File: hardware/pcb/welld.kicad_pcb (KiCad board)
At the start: 2 copper layers, 80 x 55 mm, 74 parts, among them J1 LiPo, J10 PROG, J12 Solar, J2 USB-C, J3 U.FL, J4 4-20mA_1, J5 4-20mA_2, J6 DS18B20, J7 Spare, J8 I2C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

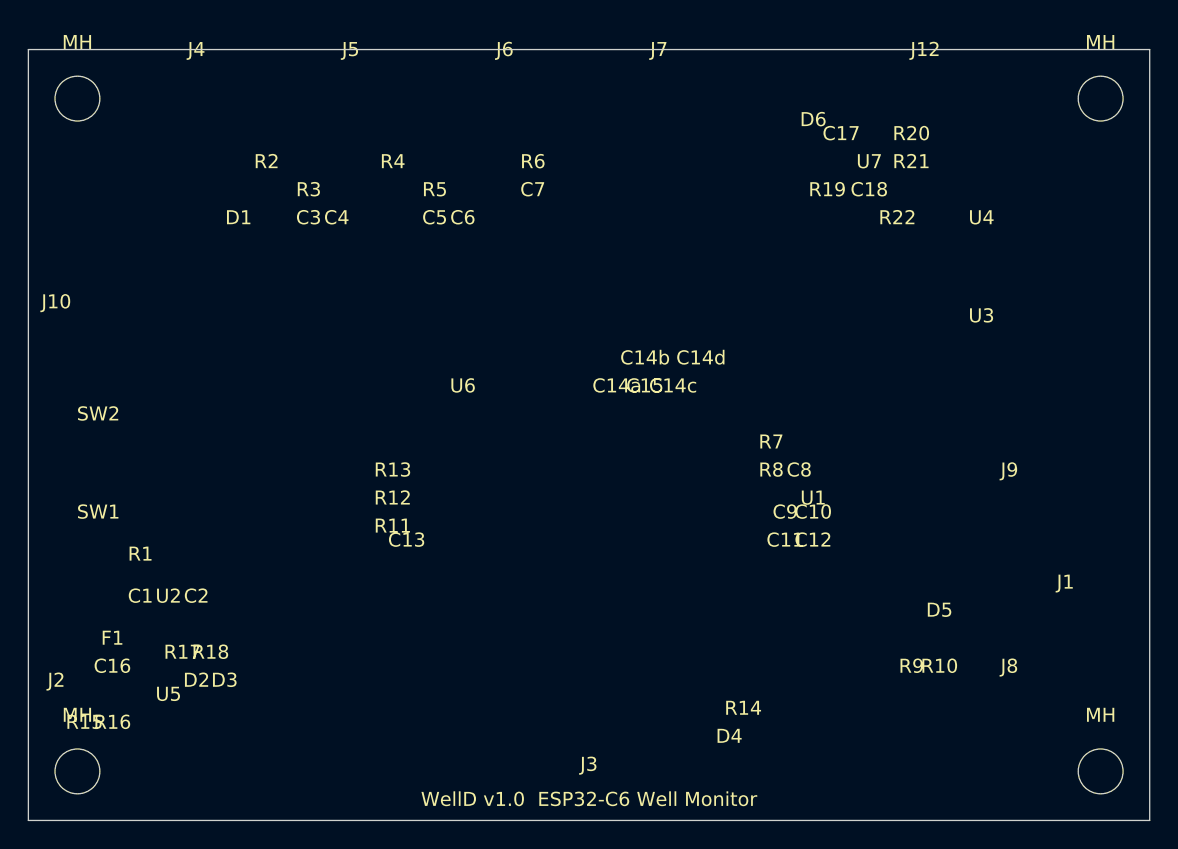
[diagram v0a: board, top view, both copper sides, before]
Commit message: Bring PCB schematic/layout in sync with the design docs
The KiCad generator was a revision behind the design notes and BOM:
the 12 V boost (U8), external ADC (U9), fuel gauge (U10), charger
interlock (Q1/Q2), boost inductor (L1), solar TVS (D8) and their
passives were documented but absent from welld.kicad_sch/.kicad_pcb.
Add them to generate_kicad.py, with TPS61023/ADS1115/MAX17048 symbols,
and regenerate.

Fix schematic/layout bugs: duplicate ESP32-C6 pin number, missing
GPIO14, stale DW01A symbol (now S-8261A), JST PH footprint on J1
(now JST XH), ADS1115 SOIC-8 footprint (now MSOP-10/VSSOP-10, the
correct 10-pin package), and two off-board component placements.
Add the missing TP4056 CE pull-up (R29).

Correct design.md errors: the R23/R24 boost-divider values, the D8
TVS protection claim, the reverse-polarity FET topology, the ESP32-C6
USB pin assignment, the ADS1115 channel/PGA description, and add a
GPIO15 strapping note and an MPPT diode-drop note.

Drop all revision language across the hardware docs and generators —
this is the single current design.

https://claude.ai/code/session_01QqBrArSSEuu1qysbVH7Nqt
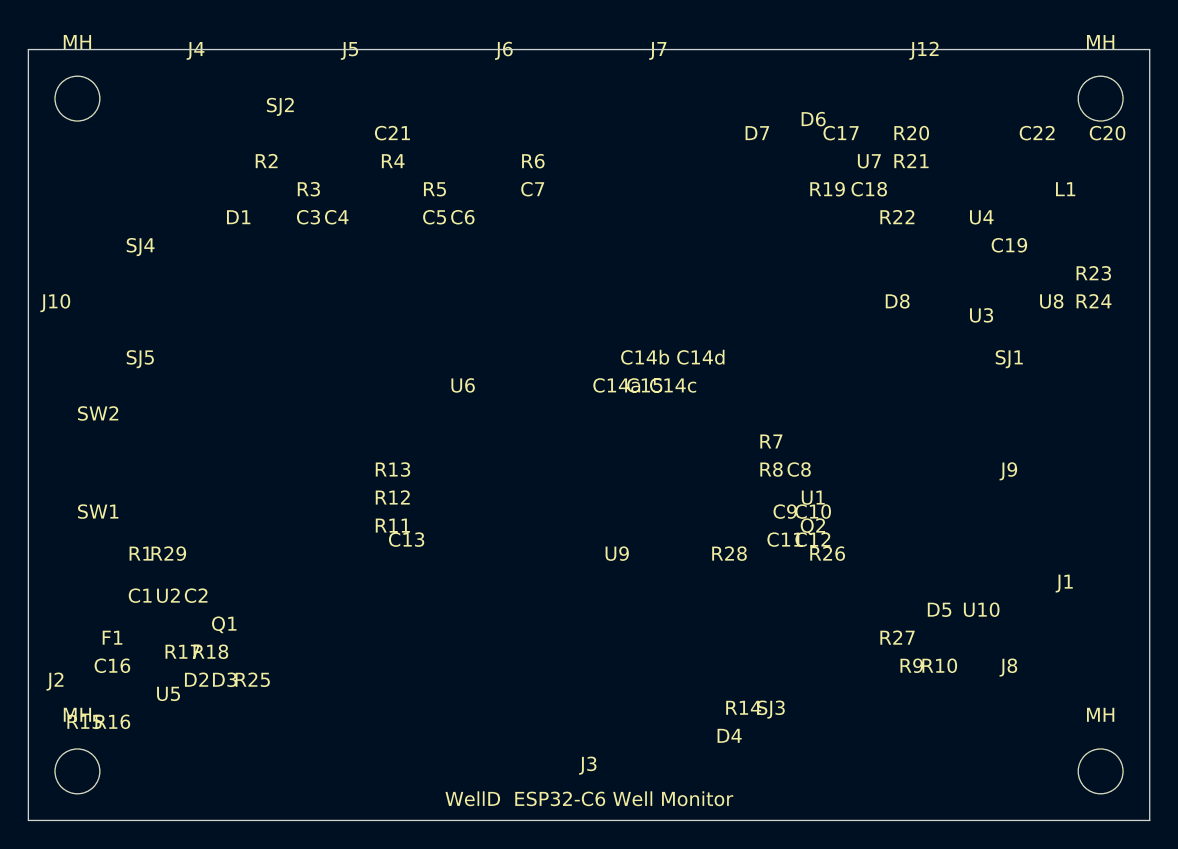
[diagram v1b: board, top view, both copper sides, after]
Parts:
- added C19: 10uF, Capacitor_SMD:C_0805_2012Metric, F.Cu at (70.0, 16.0)
- added C20: 22uF, Capacitor_SMD:C_1206_3216Metric, F.Cu at (77.0, 8.00)
- added C21: 100nF, Capacitor_SMD:C_0402_1005Metric, F.Cu at (26.0, 8.00)
- added C22: 10uF, Capacitor_SMD:C_0805_2012Metric, F.Cu at (72.0, 8.00)
- added D7: LED_SOLAR, LED_SMD:LED_0603_1608Metric, F.Cu at (52.0, 8.00)
- added D8: SMAJ7.0A, Diode_SMD:D_SMA, F.Cu at (62.0, 20.0)
- added L1: 4.7uH, Inductor_SMD:L_1812_4532Metric, F.Cu at (74.0, 12.0)
- added Q1: BSS123, Package_TO_SOT_SMD:SOT-23, F.Cu at (14.0, 43.0)
- added Q2: BSS123, Package_TO_SOT_SMD:SOT-23, F.Cu at (56.0, 36.0)
- added R23: 1.1M, Resistor_SMD:R_0402_1005Metric, F.Cu at (76.0, 18.0)
- added R24: 47k, Resistor_SMD:R_0402_1005Metric, F.Cu at (76.0, 20.0)
- added R25: 4k7, Resistor_SMD:R_0402_1005Metric, F.Cu at (16.0, 47.0)
- added R26: 4k7, Resistor_SMD:R_0402_1005Metric, F.Cu at (57.0, 38.0)
- added R27: 4k7, Resistor_SMD:R_0402_1005Metric, F.Cu at (62.0, 44.0)
- added R28: 100R, Resistor_SMD:R_0402_1005Metric, F.Cu at (50.0, 38.0)
- added R29: 4k7, Resistor_SMD:R_0402_1005Metric, F.Cu at (10.0, 38.0)
- added SJ1: VBOOST_EN, Jumper:SolderJumper-2_P1.3mm_Open_RoundedPad1.0x1.5mm, F.Cu at (70.0, 24.0)
- added SJ2: VLOOP_BUS, Jumper:SolderJumper-2_P1.3mm_Open_RoundedPad1.0x1.5mm, F.Cu at (18.0, 6.00)
- added SJ3: LED_DIS, Jumper:SolderJumper-2_P1.3mm_Open_RoundedPad1.0x1.5mm, F.Cu at (53.0, 49.0)
- added SJ4: UART_TX, Jumper:SolderJumper-2_P1.3mm_Open_RoundedPad1.0x1.5mm, F.Cu at (8.00, 16.0)
- added SJ5: UART_RX, Jumper:SolderJumper-2_P1.3mm_Open_RoundedPad1.0x1.5mm, F.Cu at (8.00, 24.0)
- added U10: MAX17048, Package_TO_SOT_SMD:SOT-23-6, F.Cu at (68.0, 42.0)
- added U8: TPS61023, Package_TO_SOT_SMD:SOT-23-5, F.Cu at (73.0, 20.0)
- added U9: ADS1115, Package_SO:MSOP-10_3x3mm_P0.5mm, F.Cu at (42.0, 38.0)
- J1: footprint Connector_JST:JST_PH_S2B-PH-K_1x02_P2.00mm_Horizontal -> Connector_JST:JST_XH_B2B-XH-AM_1x02_P2.50mm_Horizontal
- U3: value DW01A -> S-8261A
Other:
- board text added: "WellD ESP32-C6 Well Monitor"
- board text removed: "WellD v1.0 ESP32-C6 Well Monitor"
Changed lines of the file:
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@@
     (title "WellD Well-Level Monitor PCB")
     (date "2026-05-16")
-    (rev "1.0")
     (company "WellD Project")
   )
@@
   (net 22 "/CHRG_SOLAR")
   (net 23 "/DONE_SOLAR")
+  (net 24 "VLOOP")
+  (net 25 "VBOOST_EN")
+  (net 26 "CHRG_USB_DIS")
+  (net 27 "SOLAR_DET")
+  (net 28 "BATT_DIV_EN")
+  (net 29 "ADS_DRDY")
+  (net 30 "MAX_ALRT")
   (gr_line (start 0.000 0.000) (end 80.000 0.000)
     (stroke (width 0.05) (type solid)) (layer "Edge.Cuts")
@@
     (stroke (width 0.05) (type solid)) (layer "Edge.Cuts")
   )
-  (gr_text "WellD v1.0  ESP32-C6 Well Monitor" (at 40 53.5 0) (layer "F.SilkS")
+  (gr_text "WellD  ESP32-C6 Well Monitor" (at 40 53.5 0) (layer "F.SilkS")
     (effects (font (size 1.0 1.0) (thickness 0.15)))
   )
@@
       (effects (font (size 1 1) (thickness 0.15)))
     )
-    (property "Value" "DW01A" (at 0 2 0) (layer "F.Fab")
+    (property "Value" "S-8261A" (at 0 2 0) (layer "F.Fab")
       (effects (font (size 1 1) (thickness 0.15)))
     )
@@
     )
   )
-  (footprint "Connector_JST:JST_PH_S2B-PH-K_1x02_P2.00mm_Horizontal" (layer "F.Cu") (at 74.000 40.000 0.0)
+  (footprint "Connector_JST:JST_XH_B2B-XH-AM_1x02_P2.50mm_Horizontal" (layer "F.Cu") (at 74.000 40.000 0.0)
     (property "Reference" "J1" (at 0 -2 0) (layer "F.SilkS")
       (effects (font (size 1 1) (thickness 0.15)))
@@
       (effects (font (size 1 1) (thickness 0.15)))
     )
+  )
+  (footprint "Package_TO_SOT_SMD:SOT-23-5" (layer "F.Cu") (at 73.000 20.000 0.0)
+    (property "Reference" "U8" (at 0 -2 0) (layer "F.SilkS")
+      (effects (font (size 1 1) (thickness 0.15)))
+    )
+    (property "Value" "TPS61023" (at 0 2 0) (layer "F.Fab")
+      (effects (font (size 1 1) (thickness 0.15)))
+    )
+  )
+  (footprint "Inductor_SMD:L_1812_4532Metric" (layer "F.Cu") (at 74.000 12.000 0.0)
+    (property "Reference" "L1" (at 0 -2 0) (layer "F.SilkS")
+      (effects (font (size 1 1) (thickness 0.15)))
+    )
+    (property "Value" "4.7uH" (at 0 2 0) (layer "F.Fab")
+      (effects (font (size 1 1) (thickness 0.15)))
+    )
+  )
+  (footprint "Resistor_SMD:R_0402_1005Metric" (layer "F.Cu") (at 76.000 18.000 0.0)
+    (property "Reference" "R23" (at 0 -2 0) (layer "F.SilkS")
+      (effects (font (size 1 1) (thickness 0.15)))
+    )
+    (property "Value" "1.1M" (at 0 2 0) (layer "F.Fab")
+      (effects (font (size 1 1) (thickness 0.15)))
+    )
+  )
+  (footprint "Resistor_SMD:R_0402_1005Metric" (layer "F.Cu") (at 76.000 20.000 0.0)
+    (property "Reference" "R24" (at 0 -2 0) (layer "F.SilkS")
+      (effects (font (size 1 1) (thickness 0.15)))
+    )
+    (property "Value" "47k" (at 0 2 0) (layer "F.Fab")
+      (effects (font (size 1 1) (thickness 0.15)))
+    )
+  )
+  (footprint "Capacitor_SMD:C_0805_2012Metric" (layer "F.Cu") (at 70.000 16.000 0.0)
+    (property "Reference" "C19" (at 0 -2 0) (layer "F.SilkS")
+      (effects (font (size 1 1) (thickness 0.15)))
+    )
+    (property "Value" "10uF" (at 0 2 0) (layer "F.Fab")
+      (effects (font (size 1 1) (thickness 0.15)))
+    )
+  )
+  (footprint "Capacitor_SMD:C_1206_3216Metric" (layer "F.Cu") (at 77.000 8.000 0.0)
+    (property "Reference" "C20" (at 0 -2 0) (layer "F.SilkS")
+      (effects (font (size 1 1) (thickness 0.15)))
+    )
+    (property "Value" "22uF" (at 0 2 0) (layer "F.Fab")
+      (effects (font (size 1 1) (thickness 0.15)))
+    )
+  )
+  (footprint "Capacitor_SMD:C_0805_2012Metric" (layer "F.Cu") (at 72.000 8.000 0.0)
+    (property "Reference" "C22" (at 0 -2 0) (layer "F.SilkS")
+      (effects (font (size 1 1) (thickness 0.15)))
+    )
+    (property "Value" "10uF" (at 0 2 0) (layer "F.Fab")
+      (effects (font (size 1 1) (thickness 0.15)))
+    )
+  )
+  (footprint "Package_SO:MSOP-10_3x3mm_P0.5mm" (layer "F.Cu") (at 42.000 38.000 0.0)
+    (property "Reference" "U9" (at 0 -2 0) (layer "F.SilkS")
+      (effects (font (size 1 1) (thickness 0.15)))
+    )
+    (property "Value" "ADS1115" (at 0 2 0) (layer "F.Fab")
+      (effects (font (size 1 1) (thickness 0.15)))
+    )
+  )
+  (footprint "Package_TO_SOT_SMD:SOT-23-6" (layer "F.Cu") (at 68.000 42.000 0.0)
+    (property "Reference" "U10" (at 0 -2 0) (layer "F.SilkS")
+      (effects (font (size 1 1) (thickness 0.15)))
+    )
+    (property "Value" "MAX17048" (at 0 2 0) (layer "F.Fab")
+      (effects (font (size 1 1) (thickness 0.15)))
+    )
+  )
+  (footprint "Resistor_SMD:R_0402_1005Metric" (layer "F.Cu") (at 62.000 44.000 0.0)
+    (property "Reference" "R27" (at 0 -2 0) (layer "F.SilkS")
+      (effects (font (size 1 1) (thickness 0.15)))
+    )
+    (property "Value" "4k7" (at 0 2 0) (layer "F.Fab")
+      (effects (font (size 1 1) (thickness 0.15)))
+    )
+  )
+  (footprint "Resistor_SMD:R_0402_1005Metric" (layer "F.Cu") (at 50.000 38.000 0.0)
+    (property "Reference" "R28" (at 0 -2 0) (layer "F.SilkS")
+      (effects (font (size 1 1) (thickness 0.15)))
+    )
+    (property "Value" "100R" (at 0 2 0) (layer "F.Fab")
+      (effects (font (size 1 1) (thickness 0.15)))
+    )
+  )
+  (footprint "Package_TO_SOT_SMD:SOT-23" (layer "F.Cu") (at 14.000 43.000 0.0)
+    (property "Reference" "Q1" (at 0 -2 0) (layer "F.SilkS")
+      (effects (font (size 1 1) (thickness 0.15)))
+    )
+    (property "Value" "BSS123" (at 0 2 0) (layer "F.Fab")
+      (effects (font (size 1 1) (thickness 0.15)))
+    )
+  )
+  (footprint "Package_TO_SOT_SMD:SOT-23" (layer "F.Cu") (at 56.000 36.000 0.0)
+    (property "Reference" "Q2" (at 0 -2 0) (layer "F.SilkS")
+      (effects (font (size 1 1) (thickness 0.15)))
+    )
+    (property "Value" "BSS123" (at 0 2 0) (layer "F.Fab")
+      (effects (font (size 1 1) (thickness 0.15)))
+    )
+  )
+  (footprint "Resistor_SMD:R_0402_1005Metric" (layer "F.Cu") (at 16.000 47.000 0.0)
+    (property "Reference" "R25" (at 0 -2 0) (layer "F.SilkS")
+      (effects (font (size 1 1) (thickness 0.15)))
+    )
+    (property "Value" "4k7" (at 0 2 0) (layer "F.Fab")
+      (effects (font (size 1 1) (thickness 0.15)))
+    )
+  )
+  (footprint "Resistor_SMD:R_0402_1005Metric" (layer "F.Cu") (at 57.000 38.000 0.0)
+    (property "Reference" "R26" (at 0 -2 0) (layer "F.SilkS")
+      (effects (font (size 1 1) (thickness 0.15)))
+    )
+    (property "Value" "4k7" (at 0 2 0) (layer "F.Fab")
+      (effects (font (size 1 1) (thickness 0.15)))
+    )
+  )
+  (footprint "Resistor_SMD:R_0402_1005Metric" (layer "F.Cu") (at 10.000 38.000 0.0)
+    (property "Reference" "R29" (at 0 -2 0) (layer "F.SilkS")
+      (effects (font (size 1 1) (thickness 0.15)))
+    )
+    (property "Value" "4k7" (at 0 2 0) (layer "F.Fab")
+      (effects (font (size 1 1) (thickness 0.15)))
+    )
+  )
+  (footprint "LED_SMD:LED_0603_1608Metric" (layer "F.Cu") (at 52.000 8.000 0.0)
+    (property "Reference" "D7" (at 0 -2 0) (layer "F.SilkS")
+      (effects (font (size 1 1) (thickness 0.15)))
+    )
+    (property "Value" "LED_SOLAR" (at 0 2 0) (layer "F.Fab")
+      (effects (font (size 1 1) (thickness 0.15)))
+    )
+  )
+  (footprint "Diode_SMD:D_SMA" (layer "F.Cu") (at 62.000 20.000 0.0)
+    (property "Reference" "D8" (at 0 -2 0) (layer "F.SilkS")
+      (effects (font (size 1 1) (thickness 0.15)))
+    )
+    (property "Value" "SMAJ7.0A" (at 0 2 0) (layer "F.Fab")
+      (effects (font (size 1 1) (thickness 0.15)))
+    )
+  )
+  (footprint "Capacitor_SMD:C_0402_1005Metric" (layer "F.Cu") (at 26.000 8.000 0.0)
+    (property "Reference" "C21" (at 0 -2 0) (layer "F.SilkS")
+      (effects (font (size 1 1) (thickness 0.15)))
+    )
+    (property "Value" "100nF" (at 0 2 0) (layer "F.Fab")
+      (effects (font (size 1 1) (thickness 0.15)))
+    )
+  )
+  (footprint "Jumper:SolderJumper-2_P1.3mm_Open_RoundedPad1.0x1.5mm" (layer "F.Cu") (at 70.000 24.000 0.0)
+    (property "Reference" "SJ1" (at 0 -2 0) (layer "F.SilkS")
+      (effects (font (size 1 1) (thickness 0.15)))
+    )
+    (property "Value" "VBOOST_EN" (at 0 2 0) (layer "F.Fab")
+      (effects (font (size 1 1) (thickness 0.15)))
+    )
+  )
+  (footprint "Jumper:SolderJumper-2_P1.3mm_Open_RoundedPad1.0x1.5mm" (layer "F.Cu") (at 18.000 6.000 0.0)
+    (property "Reference" "SJ2" (at 0 -2 0) (layer "F.SilkS")
+      (effects (font (size 1 1) (thickness 0.15)))
+    )
+    (property "Value" "VLOOP_BUS" (at 0 2 0) (layer "F.Fab")
+      (effects (font (size 1 1) (thickness 0.15)))
+    )
+  )
+  (footprint "Jumper:SolderJumper-2_P1.3mm_Open_RoundedPad1.0x1.5mm" (layer "F.Cu") (at 53.000 49.000 0.0)
+    (property "Reference" "SJ3" (at 0 -2 0) (layer "F.SilkS")
+      (effects (font (size 1 1) (thickness 0.15)))
+    )
+    (property "Value" "LED_DIS" (at 0 2 0) (layer "F.Fab")
+      (effects (font (size 1 1) (thickness 0.15)))
+    )
+  )
+  (footprint "Jumper:SolderJumper-2_P1.3mm_Open_RoundedPad1.0x1.5mm" (layer "F.Cu") (at 8.000 16.000 0.0)
+    (property "Reference" "SJ4" (at 0 -2 0) (layer "F.SilkS")
+      (effects (font (size 1 1) (thickness 0.15)))
+    )
+    (property "Value" "UART_TX" (at 0 2 0) (layer "F.Fab")
+      (effects (font (size 1 1) (thickness 0.15)))
+    )
+  )
+  (footprint "Jumper:SolderJumper-2_P1.3mm_Open_RoundedPad1.0x1.5mm" (layer "F.Cu") (at 8.000 24.000 0.0)
+    (property "Reference" "SJ5" (at 0 -2 0) (layer "F.SilkS")
+      (effects (font (size 1 1) (thickness 0.15)))
+    )
+    (property "Value" "UART_RX" (at 0 2 0) (layer "F.Fab")
+      (effects (font (size 1 1) (thickness 0.15)))
+    )
